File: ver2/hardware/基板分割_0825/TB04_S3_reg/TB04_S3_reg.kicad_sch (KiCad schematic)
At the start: 12 parts, among them J101 USB_C_Receptacle_PowerOnly_6P, SW101 SW_SPDT, U101 74LS157, U102 74HC138

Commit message: ver2: 残り5プロジェクトの不要シートを一括削除
IF表示13/S4 10/S3 11/S1 12/S2 10枚のsheetブロックをS式単位で除去し、
対応する子シート56ファイルを削除。部分削除が要るROM_ALU・PCは残した。
残ったブロックは全てHEADとバイト一致・括弧バランス0を全数確認。

Co-Authored-By: Claude Opus 5 <noreply@anthropic.com>
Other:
- removed sheet CLK_RST
- removed sheet Decoder
- removed sheet InterFace
- removed sheet ROM_ALU
- removed sheet addrDecord
- removed sheet addrMUX
- removed sheet gates
- removed sheet inPort
- removed sheet outPort
- removed sheet ram
- removed sheet sp

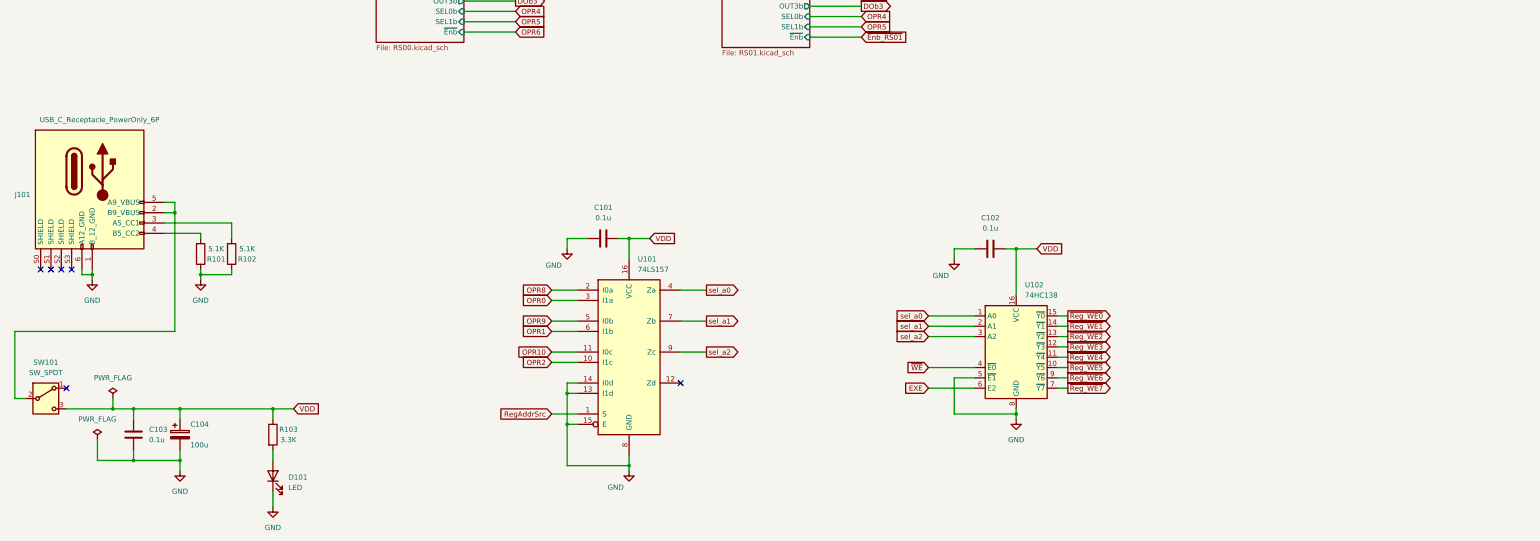
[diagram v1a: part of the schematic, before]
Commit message: ver2: S1-S4のシート内部分削除が完了(署名相違ゼロ)
ROM_ALUをS1(命令ROM側)とS2(ALU ROM・フラグ側)に、PCをS3(ALU入力MUX)と
S4(PC系)に分割。4基板1320ピンをマスターと署名比較して相違0・
ANOMALIES 0。パスコンの員数もIC数と一致(S1 7/S2 17/S3 22/S4 15)。

Co-Authored-By: Claude Opus 5 <noreply@anthropic.com>
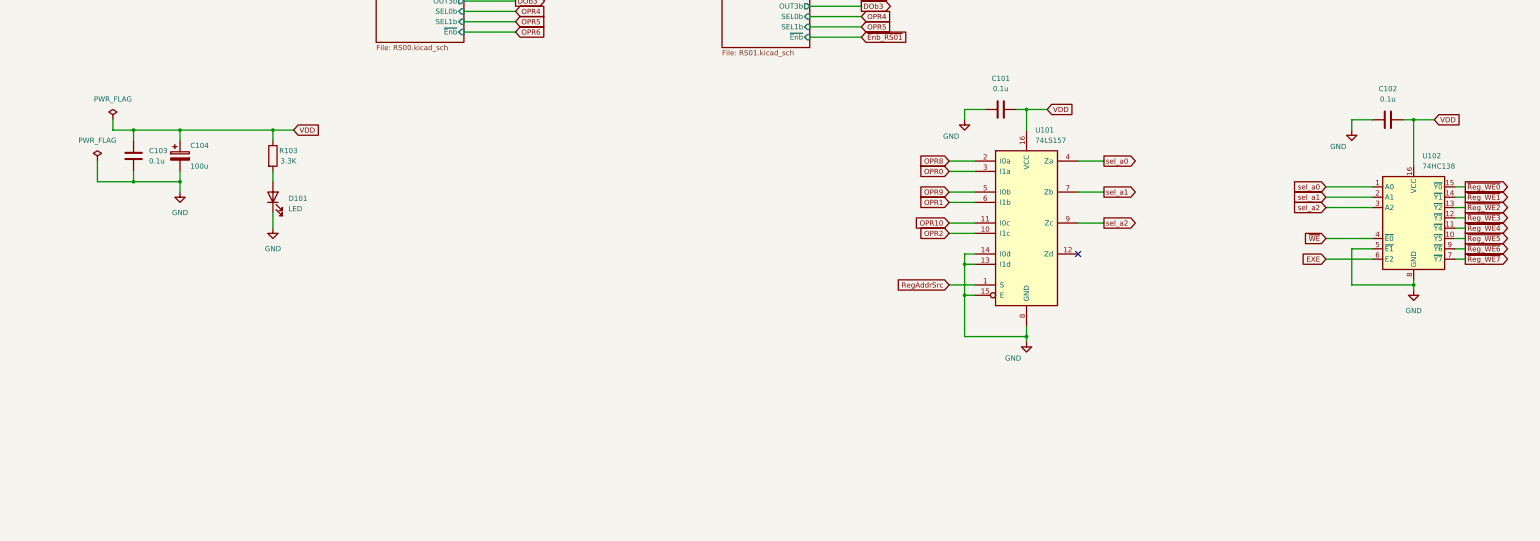
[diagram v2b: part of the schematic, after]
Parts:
- removed J101: USB_C_Receptacle_PowerOnly_6P, Library:USB_C_receptacle_onlypower_tanuki, symbol New_Library:USB_C_Receptacle_PowerOnly_6P_tanuki
- removed R101, R102: 5.1K, Resistor_THT:R_Axial_DIN0207_L6.3mm_D2.5mm_P10.16mm_Horizontal, symbol Device:R
- removed SW101: SW_SPDT, Library:sw_slide, symbol Switch:SW_SPDT
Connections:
- no-connect marks 6 -> 1
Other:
- moved on the sheet: C101, C102, C103, C104, D101, R103, U101, U102

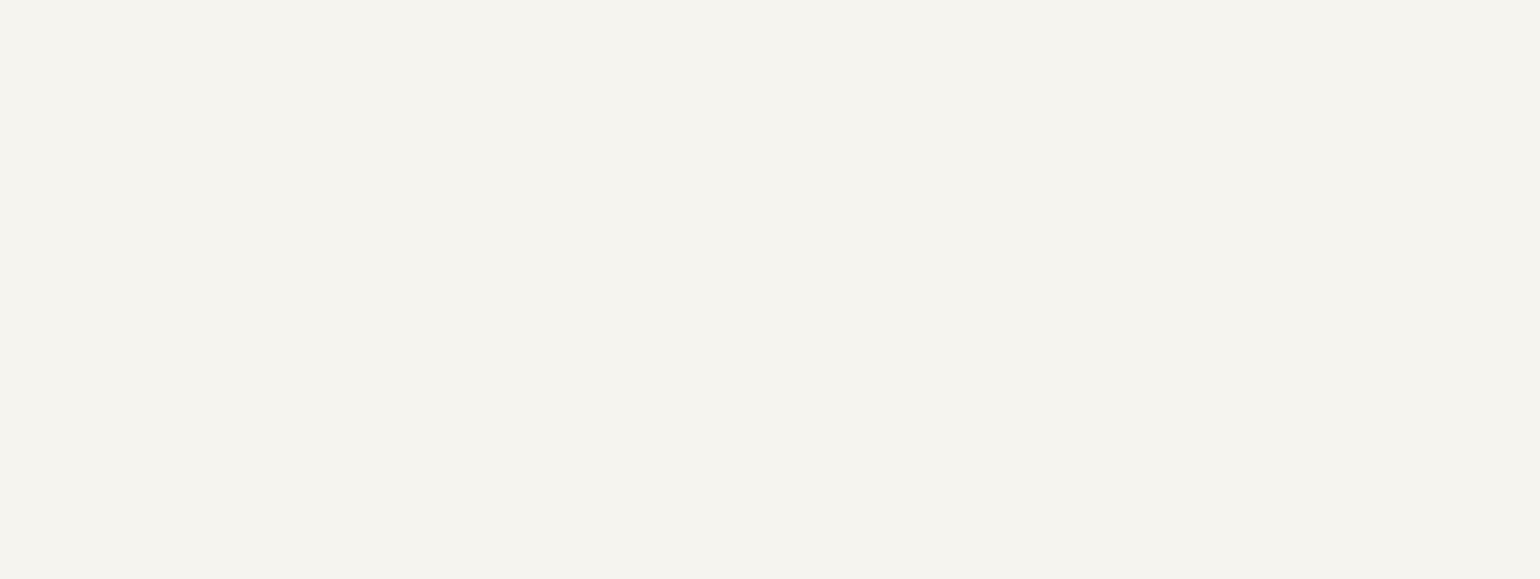
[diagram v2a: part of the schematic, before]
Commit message: ver2: S1-S4にバスヘッダ3本を実装(120ピン全数一致)／S4にIF向け20ピン3個
J101-103は4枚とも確定表と全120ピン一致。J104(IF入力)/J105(IF表示)/
J106(キャリアB)も20ピン全一致。コネクタ以外の署名はマスターと相違0で、
コネクタ追加時のワイヤ吸着なし。PC_Qはバスに載せずJ106のみ。

Co-Authored-By: Claude Opus 5 <noreply@anthropic.com>
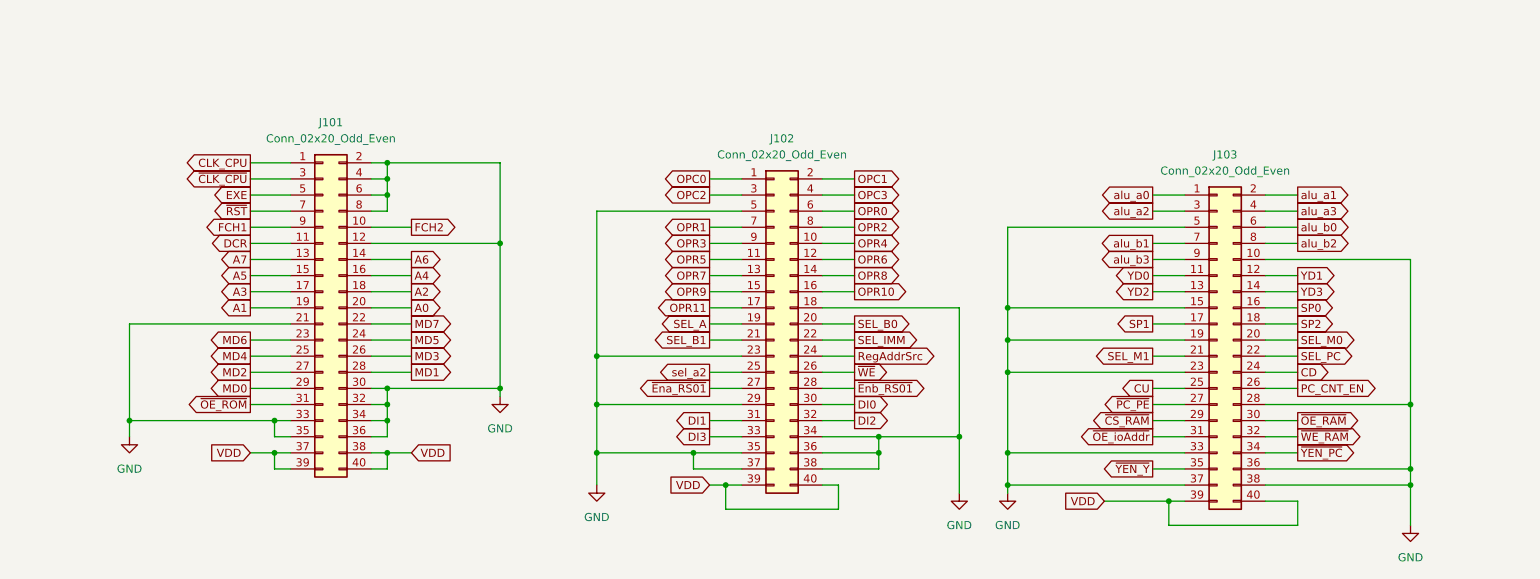
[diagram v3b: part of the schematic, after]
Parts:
- added J101, J102, J103: Conn_02x20_Odd_Even, symbol Connector_Generic:Conn_02x20_Odd_Even
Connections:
- net DI0: now also J102.30 (Pin_30)
- net DI1: now also J102.31 (Pin_31)
- net DI2: now also J102.32 (Pin_32)
- net DI3: now also J102.33 (Pin_33)
- net EXE: now also J101.5 (Pin_5)
- net GND: now also J101.12 (Pin_12), J101.2 (Pin_2), J101.21 (Pin_21), J101.30 (Pin_30), J101.32 (Pin_32), J101.33 (Pin_33), J101.34 (Pin_34), J101.35 (Pin_35), J101.36 (Pin_36), J101.4 (Pin_4), J101.6 (Pin_6), J101.8 (Pin_8), J102.18 (Pin_18), J102.23 (Pin_23), J102.29 (Pin_29), J102.34 (Pin_34), J102.35 (Pin_35), J102.36 (Pin_36), J102.37 (Pin_37), J102.38 (Pin_38), J102.5 (Pin_5), J103.10 (Pin_10), J103.15 (Pin_15), J103.19 (Pin_19), J103.23 (Pin_23), J103.28 (Pin_28), J103.33 (Pin_33), J103.36 (Pin_36), J103.37 (Pin_37), J103.38 (Pin_38), J103.5 (Pin_5)
- net OPR0: now also J102.6 (Pin_6)
- net OPR1: now also J102.7 (Pin_7)
- net OPR10: now also J102.16 (Pin_16)
- net OPR2: now also J102.8 (Pin_8)
- net OPR4: now also J102.10 (Pin_10)
- net OPR5: now also J102.11 (Pin_11)
- net OPR6: now also J102.12 (Pin_12)
- net OPR8: now also J102.14 (Pin_14)
- net OPR9: now also J102.15 (Pin_15)
- net RegAddrSrc: now also J102.24 (Pin_24)
- net VDD: now also J101.37 (Pin_37), J101.38 (Pin_38), J101.39 (Pin_39), J101.40 (Pin_40), J102.39 (Pin_39), J102.40 (Pin_40), J103.39 (Pin_39), J103.40 (Pin_40)
- net sel_a2: now also J102.25 (Pin_25)
- net ~{Ena_RS01}: now also J102.27 (Pin_27)
- net ~{Enb_RS01}: now also J102.28 (Pin_28)
- net ~{WE}: now also J102.26 (Pin_26)
- new net A0: J101.20 (Pin_20)
- new net A1: J101.19 (Pin_19)
- new net A2: J101.18 (Pin_18)
- new net A3: J101.17 (Pin_17)
- new net A4: J101.16 (Pin_16)
- new net A5: J101.15 (Pin_15)
- new net A6: J101.14 (Pin_14)
- new net A7: J101.13 (Pin_13)
- new net CD: J103.24 (Pin_24)
- new net CLK_CPU: J101.1 (Pin_1)
- new net CU: J103.25 (Pin_25)
- new net DCR: J101.11 (Pin_11)
- new net FCH1: J101.9 (Pin_9)
- new net FCH2: J101.10 (Pin_10)
- new net MD0: J101.29 (Pin_29)
- new net MD1: J101.28 (Pin_28)
- new net MD2: J101.27 (Pin_27)
- new net MD3: J101.26 (Pin_26)
- new net MD4: J101.25 (Pin_25)
- new net MD5: J101.24 (Pin_24)
- new net MD6: J101.23 (Pin_23)
- new net MD7: J101.22 (Pin_22)
- new net OPC0: J102.1 (Pin_1)
- new net OPC1: J102.2 (Pin_2)
- new net OPC2: J102.3 (Pin_3)
- new net OPC3: J102.4 (Pin_4)
- new net OPR11: J102.17 (Pin_17)
- new net OPR3: J102.9 (Pin_9)
- new net OPR7: J102.13 (Pin_13)
- new net PC_CNT_EN: J103.26 (Pin_26)
- new net SEL_A: J102.19 (Pin_19)
- new net SEL_B0: J102.20 (Pin_20)
- new net SEL_B1: J102.21 (Pin_21)
- new net SEL_IMM: J102.22 (Pin_22)
- new net SEL_M0: J103.20 (Pin_20)
- new net SEL_M1: J103.21 (Pin_21)
- new net SEL_PC: J103.22 (Pin_22)
- new net SP0: J103.16 (Pin_16)
- new net SP1: J103.17 (Pin_17)
- new net SP2: J103.18 (Pin_18)
- new net YD0: J103.11 (Pin_11)
- new net YD1: J103.12 (Pin_12)
- new net YD2: J103.13 (Pin_13)
- new net YD3: J103.14 (Pin_14)
- new net alu_a0: J103.1 (Pin_1)
- new net alu_a1: J103.2 (Pin_2)
- new net alu_a2: J103.3 (Pin_3)
- new net alu_a3: J103.4 (Pin_4)
- new net alu_b0: J103.6 (Pin_6)
- new net alu_b1: J103.7 (Pin_7)
- new net alu_b2: J103.8 (Pin_8)
- new net alu_b3: J103.9 (Pin_9)
- new net ~{CLK_CPU}: J101.3 (Pin_3)
- new net ~{CS_RAM}: J103.29 (Pin_29)
- new net ~{OE_RAM}: J103.30 (Pin_30)
- new net ~{OE_ROM}: J101.31 (Pin_31)
- new net ~{OE_ioAddr}: J103.31 (Pin_31)
- new net ~{PC_PE}: J103.27 (Pin_27)
- new net ~{RST}: J101.7 (Pin_7)
- new net ~{WE_RAM}: J103.32 (Pin_32)
- new net ~{YEN_PC}: J103.34 (Pin_34)
- new net ~{YEN_Y}: J103.35 (Pin_35)

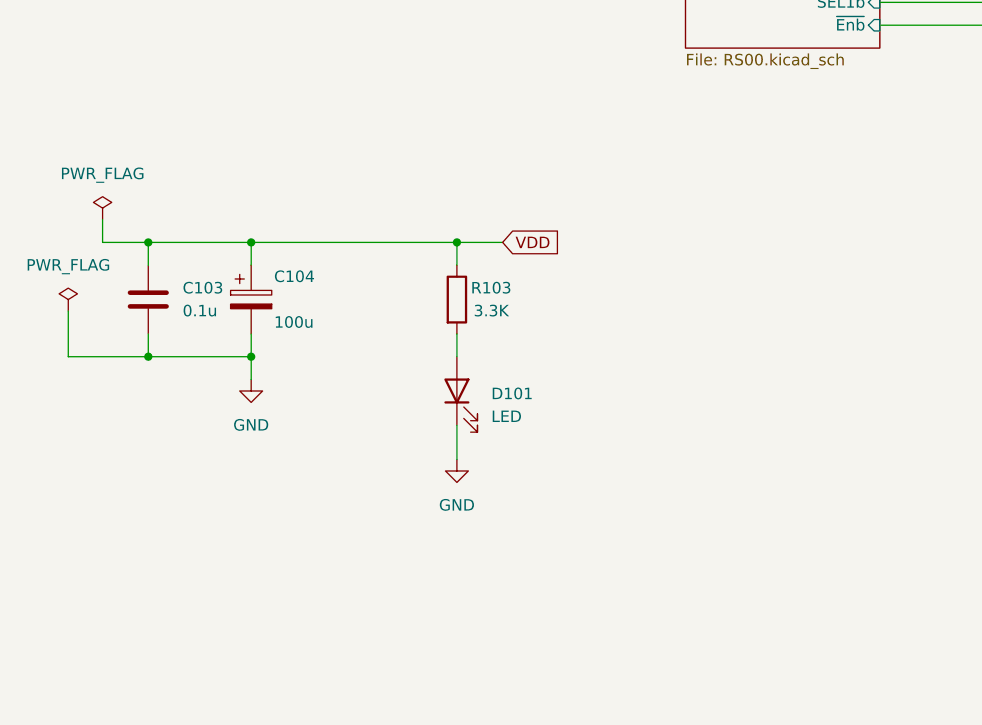
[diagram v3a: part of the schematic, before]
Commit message: ver2: キャリアに7segIF用2×5コネクタ4個と電源部を実装／全7枚に予備の端子台
- キャリア: J3-J6(2×5)が桁1-4で表と全一致・DIG_*16ネットは2ピン構成
  (isolated_pin_label 16件→0件)、C1/C2/電源LED/端子台を追加
- 入力の2×10はJ1→J2にリナンバー(20ピンの中身は表と一致)
- 7枚とも端子台J1602を1個ずつ追加(pin1=＋/pin2=GNDで向きは全枚統一)
- 署名比較で既存ピンのネット変化は7枚とも0件(吸着なし)

Co-Authored-By: Claude Opus 5 <noreply@anthropic.com>
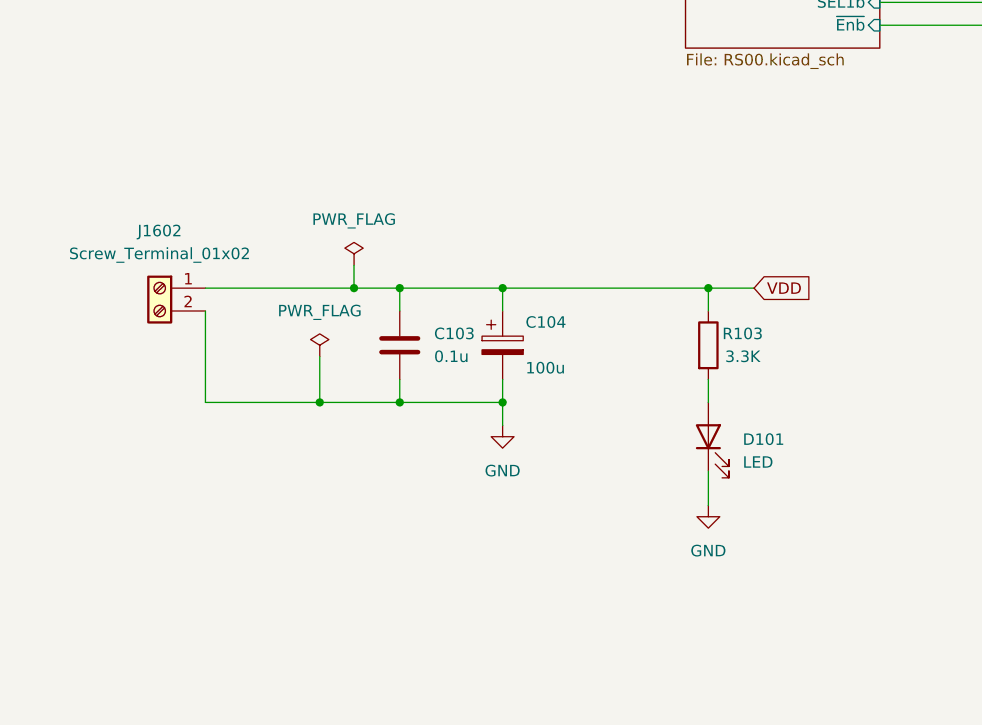
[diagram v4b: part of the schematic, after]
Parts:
- added J1602: Screw_Terminal_01x02, symbol Connector:Screw_Terminal_01x02
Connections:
- net GND: now also J1602.2 (Pin_2)
- net VDD: now also J1602.1 (Pin_1)
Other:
- moved on the sheet: C103, C104, D101, R103
